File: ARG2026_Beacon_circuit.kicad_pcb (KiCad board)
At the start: 2 copper layers, 266.2 x 125.7 mm, 21 parts, among them J1 Conn_01x02_Pin, J2 Conn_01x02_Pin, Q1 IRLML0030, U1 CH32V002A4M6

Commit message: I
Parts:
- added REF**: MountingHole_3.2mm_M3, MountingHole:MountingHole_3.2mm_M3, F.Cu at (103.0, 181.4)
- added REF**: MountingHole_3.2mm_M3, MountingHole:MountingHole_3.2mm_M3, F.Cu at (81.0, 143.3)
- added REF**: MountingHole_3.2mm_M3, MountingHole:MountingHole_3.2mm_M3, F.Cu at (147.0, 181.4)
- added REF**: MountingHole_3.2mm_M3, MountingHole:MountingHole_3.2mm_M3, F.Cu at (169.0, 143.3)
- added REF**: MountingHole_3.2mm_M3, MountingHole:MountingHole_3.2mm_M3, F.Cu at (103.0, 105.3)
- added REF**: MountingHole_3.2mm_M3, MountingHole:MountingHole_3.2mm_M3, F.Cu at (147.0, 105.2)
- moved U1 92.6 mm to (150.7, 145.1)
- moved R4 91.8 mm to (143.9, 153.7)
- moved J1 91.0 mm to (151.7, 133.2)
- moved D1 90.3 mm to (91.9, 123.0)
- moved R1 90.3 mm to (101.1, 131.2)
- moved R5 90.3 mm to (96.3, 138.6)
- moved R6 90.3 mm to (90.3, 138.5)
- moved BT1 90.3 mm to (124.5, 136.9)
- moved C1 90.3 mm to (126.2, 173.3)
- moved C2 90.3 mm to (101.1, 141.1)
- moved D2 90.3 mm to (123.3, 105.1)
- moved D4 90.3 mm to (158.4, 161.4)
- moved D5 90.3 mm to (125.8, 181.6)
- moved R2 90.3 mm to (145.4, 121.7)
- moved R3 90.3 mm to (145.4, 128.6)
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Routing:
- net GND: track 0.00 -> 113.1 mm
- net /VDD: track 25.1 -> 122.9 mm
- net Net-(D1-K): track 121.9 -> 212.4 mm
- net Net-(D5-A): track 0.00 -> 44.0 mm
- net Net-(Q1-G): track 0.00 -> 19.5 mm
- net /T1C3: track 0.00 -> 12.0 mm
- net Net-(D4-A): track 0.00 -> 11.1 mm
- net /SWIO: track 0.00 -> 9.91 mm
- added copper zone on F.Cu, net GND
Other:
- board size 266.2 x 125.7 mm -> 100 x 86.6 mm

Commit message: message
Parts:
- removed the REF** at (103.0, 181.4)
- removed the REF** at (81.0, 143.3)
- removed the REF** at (147.0, 181.4)
- removed the REF** at (169.0, 143.3)
- removed the REF** at (103.0, 105.3)
- removed the REF** at (147.0, 105.2)
- added D7: LED, LED_THT:LED_D3.0mm, F.Cu at (200.2, 94.6)
- added R9: 1k, Resistor_THT:R_Axial_DIN0207_L6.3mm_D2.5mm_P10.16mm_Horizontal, F.Cu at (192.1, 94.0)
- added REF**: MountingHole_3.2mm_M3, MountingHole:MountingHole_3.2mm_M3, F.Cu at (244.1, 61.3)
- added REF**: MountingHole_3.2mm_M3, MountingHole:MountingHole_3.2mm_M3, F.Cu at (198.1, 140.9)
- added REF**: MountingHole_3.2mm_M3, MountingHole:MountingHole_3.2mm_M3, F.Cu at (267.1, 101.1)
- added REF**: MountingHole_3.2mm_M3, MountingHole:MountingHole_3.2mm_M3, F.Cu at (198.1, 61.3)
- added REF**: MountingHole_3.2mm_M3, MountingHole:MountingHole_3.2mm_M3, F.Cu at (244.1, 140.9)
- added REF**: MountingHole_3.2mm_M3, MountingHole:MountingHole_3.2mm_M3, F.Cu at (175.1, 101.1)
- added SW1: SW_SPDT, Button_Switch_THT:SW_Slide-03_Wuerth-WS-SLTV_10x2.5x6.4_P2.54mm, F.Cu at (197.6, 108.7)
- moved C2 112.1 mm to (200.5, 89.2), turned to 180 degrees
- moved R1 106.9 mm to (198.0, 86.2), turned to 90 degrees
- moved D1 104.9 mm to (188.0, 80.8)
- moved D2 104.9 mm to (219.4, 62.9)
- moved C1 104.9 mm to (222.3, 131.1)
- moved D4 104.9 mm to (254.5, 119.2)
- moved D5 104.9 mm to (221.9, 139.4)
- moved J1 104.9 mm to (247.8, 91.0)
- moved J2 104.9 mm to (247.8, 94.9)
- moved Q1 104.9 mm to (241.6, 130.3)
- moved R2 104.9 mm to (241.5, 79.5)
- moved R3 104.9 mm to (241.5, 86.5)
- moved R4 104.9 mm to (240.0, 111.6)
- moved R8 104.9 mm to (240.0, 115.2)
- moved U1 104.9 mm to (246.8, 103.0)
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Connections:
- BT1 pad 1: /VDD -> Net-(BT1-+)
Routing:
- net Net-(BT1-+): track 0.00 -> 35.7 mm
- net /VDD: track 122.9 -> 135.5 mm
- net Net-(D7-A): track 0.00 -> 11.9 mm
- net GND: track 113.1 -> 121.7 mm
- net Net-(D1-A): track 6.12 -> 14.1 mm
- net Net-(D5-A): track 44.0 -> 51.7 mm
- net Net-(D6-A): track 12.9 -> 17.3 mm

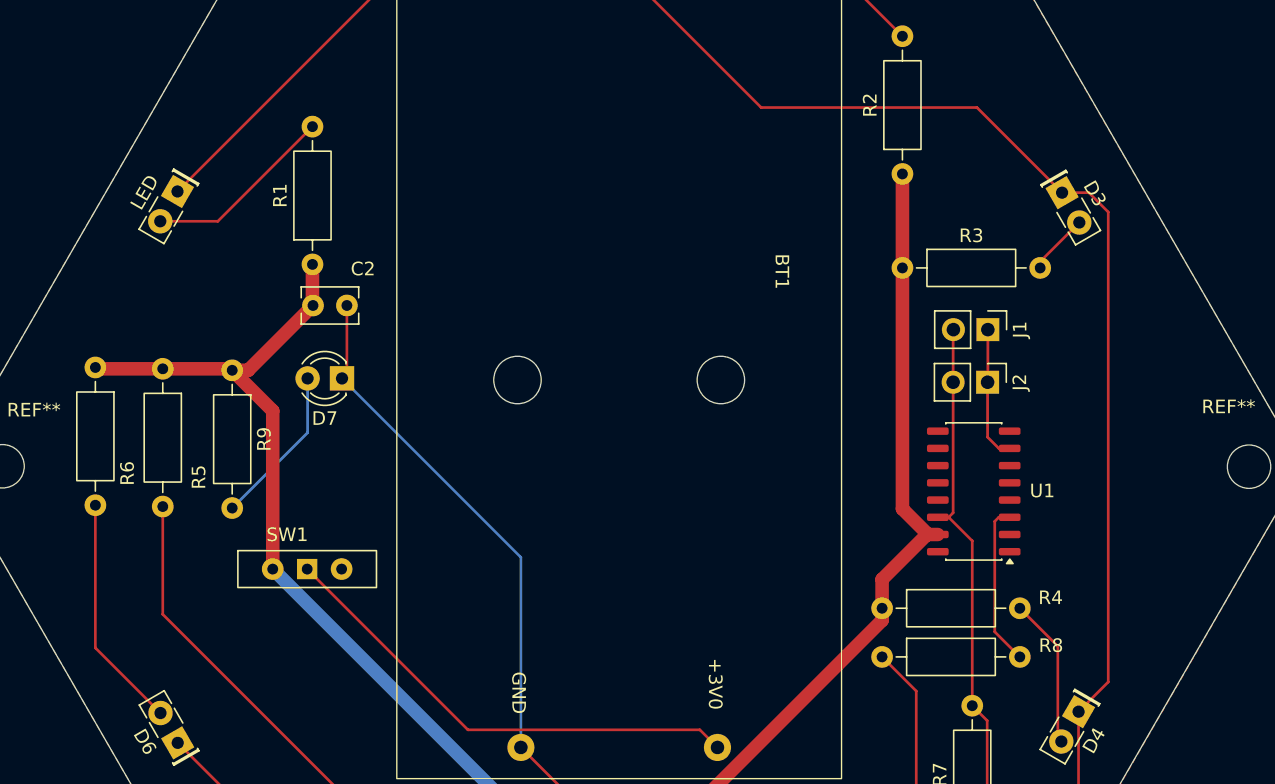
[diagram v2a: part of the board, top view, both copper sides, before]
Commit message: シルクスクリーンに値を追加、チェック
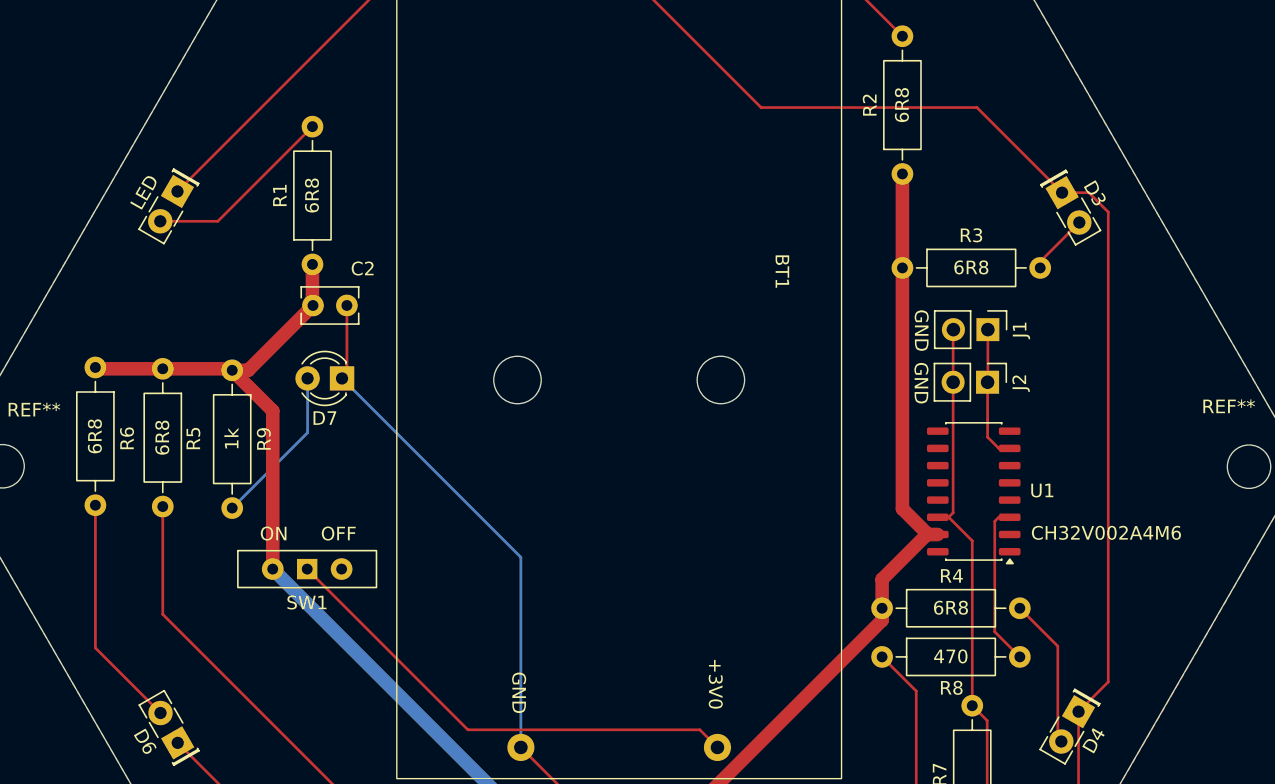
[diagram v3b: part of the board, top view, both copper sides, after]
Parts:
- R1, R2, R3, R4, R5, R6: value 5R1 -> 6R8
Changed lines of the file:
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@@
 		)
 		(property "Value" "CH32V002A4M6"
-			(at 0 5.9 0)
-			(layer "F.Fab")
+			(at -9.79 -3.09 0)
+			(layer "F.SilkS")
 			(effects
 				(font
@@
 		(tags "Resistor Axial_DIN0207 series Axial Horizontal pin pitch 10.16mm 0.25W = 1/4W length 6.3mm diameter 2.5mm")
 		(property "Reference" "R8"
-			(at 12.46 -0.83 0)
+			(at 5.12 2.316937 0)
 			(layer "F.SilkS")
 			(effects
@@
 		)
 		(property "Value" "470"
-			(at 12.78 0.93 0)
-			(layer "F.Fab")
+			(at 5.08 0 0)
+			(layer "F.SilkS")
 			(effects
 				(font
@@
 		)
 		(property "Value" "1k"
-			(at 2 -2.44 90)
-			(layer "F.Fab")
+			(at 5.08 0 90)
+			(layer "F.SilkS")
 			(effects
 				(font
@@
 			)
 		)
-		(property "Value" "5R1"
-			(at 5.08 2.37 90)
-			(layer "F.Fab")
+		(property "Value" "6R8"
+			(at 5.08 0 90)
+			(layer "F.SilkS")
 			(effects
 				(font
@@
 			(layer "F.Fab")
 		)
+		(fp_text user "GND"
+			(at -1.5 5.5 270)
+			(unlocked yes)
+			(layer "F.SilkS")
+			(effects
+				(font
+					(size 1 1)
+					(thickness 0.1)
+				)
+				(justify left bottom)
+			)
+		)
 		(fp_text user "${REFERENCE}"
 			(at 0 1.27 0)
@@
 		(tags "Resistor Axial_DIN0207 series Axial Horizontal pin pitch 10.16mm 0.25W = 1/4W length 6.3mm diameter 2.5mm")
 		(property "Reference" "R4"
-			(at 12.43 -0.77 0)
+			(at 5.12 -2.348063 0)
 			(layer "F.SilkS")
 			(effects
@@
 			)
 		)
-		(property "Value" "5R1"
-			(at 12.88 0.95 0)
-			(layer "F.Fab")
+		(property "Value" "6R8"
+			(at 5.08 0 0)
+			(layer "F.SilkS")
 			(effects
 				(font
@@
 		(tags "Resistor Axial_DIN0207 series Axial Horizontal pin pitch 10.16mm 0.25W = 1/4W length 6.3mm diameter 2.5mm")
 		(property "Reference" "R5"
-			(at 7.99 -2.67 270)
+			(at 5.15 -2.29 90)
 			(layer "F.SilkS")
 			(effects
@@
 			)
 		)
-		(property "Value" "5R1"
-			(at 3.52 -2.47 270)
-			(layer "F.Fab")
+		(property "Value" "6R8"
+			(at 5.08 0 90)
+			(layer "F.SilkS")
 			(effects
 				(font
@@
 		)
 		(property "Datasheet" ""
-			(at 0 0 270)
+			(at 0 0 90)
 			(layer "F.Fab")
 			(hide yes)
@@
 		)
 		(property "Description" "Resistor"
-			(at 0 0 270)
+			(at 0 0 90)
 			(layer "F.Fab")
 			(hide yes)
@@
 		)
 		(property "KiLib_Generator" "resistor/THT"
-			(at 0 0 270)
+			(at 0 0 90)
 			(layer "F.SilkS")
 			(hide yes)
@@
 		)
 		(fp_text user "${REFERENCE}"
-			(at 5.08 0 270)
+			(at 5.08 0 90)
 			(layer "F.Fab")
 			(effects
@@
 		(descr "Through hole straight pin header, 1x02, 2.54mm pitch, single row")
 		(tags "Through hole pin header THT 1x02 2.54mm single row")
-		(property "Reference" "J1"
-			(at 0 -2.38 90)
-			(layer "F.SilkS")
-			(effects
-				(font
-					(size 1 1)
-					(thickness 0.15)
-				)
-			)
-		)
 		(property "Value" "Conn_01x02_Pin"
 			(at 0 4.92 90)
@@
 			)
 		)
+		(property "Reference" "J1"
+			(at 0 -2.38 90)
+			(layer "F.SilkS")
+			(effects
+				(font
+					(size 1 1)
+					(thickness 0.15)
+				)
+			)
+		)
 		(property ki_fp_filters "Connector*:*_1x??_*")
 		(sheetname "/")
@@
 			(layer "F.Fab")
 		)
+		(fp_text user "GND"
+			(at -1.5 5.5 270)
+			(unlocked yes)
+			(layer "F.SilkS")
+			(effects
+				(font
+					(size 1 1)
+					(thickness 0.1)
+				)
+				(justify left bottom)
+			)
+		)
 		(fp_text user "${REFERENCE}"
 			(at 0 1.27 0)
@@
 		(tags "switch single-pole opposite-side-connection double-throw SPDT würth wurth")
 		(property "Reference" "SW1"
-			(at -1.47 -2.53 0)
+			(at 0 2.5 0)
 			(layer "F.SilkS")
 			(effects
@@
 			(layer "F.Fab")
 		)
+		(fp_text user "ON"
+			(at -3.5 -2 0)
+			(unlocked yes)
+			(layer "F.SilkS")
+			(effects
+				(font
+					(size 1 1)
+					(thickness 0.1)
+				)
+				(justify left bottom)
+			)
+		)
+		(fp_text user "OFF"
+			(at 1 -2 0)
+			(unlocked yes)
+			(layer "F.SilkS")
+			(effects
+				(font
+					(size 1 1)
+					(thickness 0.1)
+				)
+				(justify left bottom)
+			)
+		)
 		(fp_text user "${REFERENCE}"
 			(at 3.6 -2.54 0)
@@
 		(tags "Resistor Axial_DIN0207 series Axial Horizontal pin pitch 10.16mm 0.25W = 1/4W length 6.3mm diameter 2.5mm")
 		(property "Reference" "R6"
-			(at 7.81 -2.37 270)
+			(at 5.25 -2.37 90)
 			(layer "F.SilkS")
 			(effects
@@
 			)
 		)
-		(property "Value" "5R1"
-			(at 3.81 -2.38 270)
-			(layer "F.Fab")
+		(property "Value" "6R8"
+			(at 5.08 0 90)
+			(layer "F.SilkS")
 			(effects
 				(font
@@
 		)
 		(property "Datasheet" ""
-			(at 0 0 270)
+			(at 0 0 90)
 			(layer "F.Fab")
 			(hide yes)
@@
 		)
 		(property "Description" "Resistor"
-			(at 0 0 270)
+			(at 0 0 90)
 			(layer "F.Fab")
 			(hide yes)
@@
 		)
 		(property "KiLib_Generator" "resistor/THT"
-			(at 0 0 270)
+			(at 0 0 90)
 			(layer "F.SilkS")
 			(hide yes)
@@
 		)
 		(fp_text user "${REFERENCE}"
-			(at 5.08 0 270)
+			(at 5.08 0 90)
 			(layer "F.Fab")
 			(effects
@@
 			)
 		)
-		(property "Value" "5R1"
-			(at 5.08 2.37 90)
-			(layer "F.Fab")
+		(property "Value" "6R8"
+			(at 5.08 0 90)
+			(layer "F.SilkS")
 			(effects
 				(font
@@
 			)
 		)
-		(property "Value" "5R1"
-			(at 5.08 2.37 0)
-			(layer "F.Fab")
+		(property "Value" "6R8"
+			(at 5.08 0 0)
+			(layer "F.SilkS")
 			(effects
 				(font

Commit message: message
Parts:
- moved R7 30.7 mm to (261.5, 102.1), turned to 180 degrees
- moved C1 30.1 mm to (196.1, 116.2), turned to 0 degrees
- moved R8 23.6 mm to (261.4, 105.3), turned to 180 degrees
- moved Q1 14.3 mm to (245.2, 116.4)
- moved J1 13.3 mm to (246.6, 104.3)
- moved J2 13.3 mm to (246.6, 108.2)
- moved U1 8.24 mm to (245.2, 94.9)
- moved R4 1.45 mm to (241.2, 112.4)
- moved BT1 0.46 mm to (220.9, 95.0)
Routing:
- net GND: track 121.7 -> 109.4 mm
- net /VDD: track 135.5 -> 124.0 mm
- net /SWIO: track 9.91 -> 17.5 mm
- net Net-(D1-K): track 212.1 -> 205.0 mm
- net Net-(Q1-G): track 19.5 -> 22.8 mm
- net Net-(BT1-+): track 35.7 -> 38.0 mm
- net /T1C3: track 12.0 -> 10.5 mm
- net Net-(D4-A): track 11.1 -> 9.75 mm
- net Net-(D5-A): track 51.7 -> 52.6 mm

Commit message: improve silkscreen of PCB
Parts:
- added ?: , clipboard:8ea2c0b2-452e-4bc2-b55e-ed6b78fbe1c2, F.Cu at (199.4, 94.6)
- C1: value 470 -> 470u
- renumbered J2 to SWIO, J1 to SWIO

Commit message: 警告
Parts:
- moved ? 2.94 mm to (199.2, 97.5)
- moved D1 2.48 mm to (186.8, 83.0), turned to 60 degrees
- renumbered SWIO to J1, SWIO to J2
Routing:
- net Net-(D1-A): track 14.1 -> 11.9 mm
- net Net-(D1-K): track 205.0 -> 207.1 mm
- removed copper zone on F.Cu, net GND
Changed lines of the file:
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@@
 	(footprint "LED_THT:LED_Rectangular_W5.0mm_H2.0mm"
 		(layer "F.Cu")
-		(at 188.024997 80.83059 -120)
+		(at 186.815 82.999852 60)
 		(descr "LED, Rectangular, size 5.0x2.0mm, 2 pins, http://www.kingbright.com/attachments/file/psearch/000/00/00/L-169XCGDK(Ver.9B).pdf, generated by kicad-footprint-generator")
 		(tags "LED")
@@
 		)
 		(property "Sim.Pins" "1=K 2=A"
-			(at 0 0 240)
+			(at 0 0 60)
 			(unlocked yes)
 			(layer "F.Fab")
@@
 		(sheetname "/")
 		(sheetfile "ARG2026_Beacon_circuit.kicad_sch")
+		(units
+			(unit
+				(name "A")
+				(pins "1" "2")
+			)
+		)
 		(attr through_hole)
 		(duplicate_pad_numbers_are_jumpers no)
 		(fp_line
-			(start 3.83 1.06)
-			(end 2.747 1.06)
+			(start -1.29 -1.06)
+			(end -1.08 -1.06)
 			(stroke
 				(width 0.12)
@@
 		)
 		(fp_line
-			(start 2.333 1.06)
-			(end 1.08 1.06)
+			(start -1.17 -1.06)
+			(end -1.17 1.06)
 			(stroke
 				(width 0.12)
@@
 		)
 		(fp_line
-			(start 0.551733 2)
-			(end 0.551733 2.448267)
+			(start 1.08 -1.06)
+			(end 2.333 -1.06)
 			(stroke
-				(width 0.070576)
-				(type default)
+				(width 0.12)
+				(type solid)
 			)
 			(layer "F.SilkS")
 		)
 		(fp_line
-			(start 0.551733 2)
-			(end 0.103404 2)
+			(start -1.29 1.06)
+			(end -1.29 -1.06)
 			(stroke
-				(width 0.070576)
-				(type default)
+				(width 0.12)
+				(type solid)
 			)
 			(layer "F.SilkS")
 		)
 		(fp_line
-			(start 0.551733 2)
-			(end 0.551733 1.551733)
+			(start -1.08 1.06)
+			(end -1.29 1.06)
 			(stroke
-				(width 0.070576)
-				(type default)
+				(width 0.12)
+				(type solid)
 			)
 			(layer "F.SilkS")
 		)
 		(fp_line
-			(start 0.103404 2)
-			(end -0.344889 2)
+			(start 2.747 -1.06)
+			(end 3.83 -1.06)
 			(stroke
-				(width 0.070576)
-				(type default)
+				(width 0.12)
+				(type solid)
 			)
 			(layer "F.SilkS")
 		)
 		(fp_line
-			(start -0.344889 2)
-			(end 2.344888 2)
+			(start 3.83 -1.06)
+			(end 3.83 1.06)
 			(stroke
-				(width 0.070576)
-				(type default)
+				(width 0.12)
+				(type solid)
 			)
 			(layer "F.SilkS")
 		)
 		(fp_line
-			(start 3.83 -1.06)
-			(end 3.83 1.06)
+			(start -0.344889 2)
+			(end 2.344888 2)
 			(stroke
-				(width 0.12)
-				(type solid)
+				(width 0.070576)
+				(type default)
 			)
 			(layer "F.SilkS")
 		)
 		(fp_line
-			(start 2.747 -1.06)
-			(end 3.83 -1.06)
+			(start 0.103404 2)
+			(end -0.344889 2)
 			(stroke
-				(width 0.12)
-				(type solid)
+				(width 0.070576)
+				(type default)
 			)
 			(layer "F.SilkS")
 		)
 		(fp_line
-			(start -1.08 1.06)
-			(end -1.29 1.06)
+			(start 0.551733 2)
+			(end 0.551733 1.551733)
 			(stroke
-				(width 0.12)
-				(type solid)
+				(width 0.070576)
+				(type default)
 			)
 			(layer "F.SilkS")
 		)
 		(fp_line
-			(start -1.29 1.06)
-			(end -1.29 -1.06)
+			(start 0.551733 2)
+			(end 0.103404 2)
 			(stroke
-				(width 0.12)
-				(type solid)
+				(width 0.070576)
+				(type default)
 			)
 			(layer "F.SilkS")
 		)
 		(fp_line
-			(start 1.08 -1.06)
-			(end 2.333 -1.06)
+			(start 0.551733 2)
+			(end 0.551733 2.448267)
 			(stroke
-				(width 0.12)
-				(type solid)
+				(width 0.070576)
+				(type default)
 			)
 			(layer "F.SilkS")
 		)
 		(fp_line
-			(start -1.17 -1.06)
-			(end -1.17 1.06)
+			(start 2.333 1.06)
+			(end 1.08 1.06)
 			(stroke
 				(width 0.12)
@@
 		)
 		(fp_line
-			(start -1.29 -1.06)
-			(end -1.08 -1.06)
+			(start 3.83 1.06)
+			(end 2.747 1.06)
 			(stroke
 				(width 0.12)
@@
 		)
 		(point
-			(at 187.389997 81.930442)
+			(at 187.45 81.9)
 			(size 2)
 			(layer "F.Fab")
 		)
 		(pad "1" thru_hole rect
-			(at 0 0 240)
+			(at 0 0 60)
 			(size 1.8 1.8)
 			(drill 0.9)
@@
 		)
 		(pad "2" thru_hole circle
-			(at 2.54 0 240)
+			(at 2.54 0 60)
 			(size 1.8 1.8)
 			(drill 0.9)
@@
 		(sheetname "/")
 		(sheetfile "ARG2026_Beacon_circuit.kicad_sch")
+		(units
+			(unit
+				(name "A")
+				(pins "1" "2")
+			)
+		)
 		(attr through_hole)
 		(duplicate_pad_numbers_are_jumpers no)
@@
 		)
 		(fp_text user "${REFERENCE}"
-			(at 1.27 0 0)
+			(at -2.37 0.04 0)
 			(layer "F.Fab")
 			(effects
@@
 	(footprint "clipboard:8ea2c0b2-452e-4bc2-b55e-ed6b78fbe1c2"
 		(layer "F.Cu")
-		(at 199.39 94.615 180)
+		(at 199.238267 97.55 180)
 		(property "Reference" ""
 			(at 0 0 0)
@@
 		(descr "Through hole straight pin header, 1x02, 2.54mm pitch, single row")
 		(tags "Through hole pin header THT 1x02 2.54mm single row")
-		(property "Reference" "SWIO"
+		(property "Reference" "J2"
 			(at 0 -2.38 90)
 			(layer "F.SilkS")
@@
 		(sheetname "/")
 		(sheetfile "ARG2026_Beacon_circuit.kicad_sch")
+		(units
+			(unit
+				(name "A")
+				(pins "1" "2")
+			)
+		)
 		(attr through_hole)
 		(duplicate_pad_numbers_are_jumpers no)
@@
 		(descr "Through hole straight pin header, 1x02, 2.54mm pitch, single row")
 		(tags "Through hole pin header THT 1x02 2.54mm single row")
-		(property "Reference" "SWIO"
+		(property "Reference" "J1"
 			(at 0 -2.38 90)
 			(layer "F.SilkS")
@@
 		(sheetname "/")
 		(sheetfile "ARG2026_Beacon_circuit.kicad_sch")
+		(units
+			(unit
+				(name "A")
+				(pins "1" "2")
+			)
+		)
 		(attr through_hole)
 		(duplicate_pad_numbers_are_jumpers no)
@@
 		)
 		(fp_text user "${REFERENCE}"
-			(at 1.27 0 60)
+			(at -2.407271 0.027042 60)
 			(layer "F.Fab")
 			(effects
@@
 		(sheetname "/")
 		(sheetfile "ARG2026_Beacon_circuit.kicad_sch")
+		(units
+			(unit
+				(name "A")
+				(pins "1" "2")
+			)
+		)
 		(attr through_hole)
 		(duplicate_pad_numbers_are_jumpers no)
@@
 		)
 		(fp_text user "${REFERENCE}"
-			(at 1.27 0 120)
+			(at 5.213768 0.129193 120)
 			(layer "F.Fab")
 			(effects
@@
 		(sheetname "/")
 		(sheetfile "ARG2026_Beacon_circuit.kicad_sch")
+		(units
+			(unit
+				(name "A")
+				(pins "1" "2")
+			)
+		)
 		(attr through_hole)
 		(duplicate_pad_numbers_are_jumpers no)
@@
 		)
 		(fp_text user "${REFERENCE}"
-			(at 1.27 0 120)
+			(at -2.511588 -0.517242 120)
 			(layer "F.Fab")
 			(effects
@@
 		(tags "LED")
 		(property "Reference" "D7"
-			(at 1.27 -2.96 0)
+			(at -2.41 0.75 0)
 			(layer "F.SilkS")
 			(effects
@@
 	)
 	(segment
-		(start 188.024997 80.83059)
-		(end 205.925587 62.93)
+		(start 219.36 62.93)
+		(end 219.36 64.91)
 		(width 0.5)
 		(layer "F.Cu")
@@
 	)
 	(segment
-		(start 219.36 62.93)
-		(end 219.36 64.91)
+		(start 199.290148 82.999852)
+		(end 186.815 82.999852)
 		(width 0.5)
 		(layer "F.Cu")
@@
 	)
 	(segment
-		(start 205.925587 62.93)
-		(end 219.36 62.93)
+		(start 219.36 62.93)
+		(end 199.290148 82.999852)
 		(width 0.5)
 		(layer "F.Cu")
@@
 	)
 	(segment
-		(start 190.999705 83.030295)
-		(end 197.98 76.05)
-		(width 1.5)
+		(start 188.085 80.800147)
+		(end 193.229853 80.800147)
+		(width 1)
 		(layer "F.Cu")
 		(net "Net-(D1-A)")
 	)
 	(segment
-		(start 186.754997 83.030295)
-		(end 190.999705 83.030295)
-		(width 1.5)
+		(start 193.229853 80.800147)
+		(end 197.98 76.05)
+		(width 1)
 		(layer "F.Cu")
 		(net "Net-(D1-A)")
@@
 	)
 	(zone
-		(net "GND")
-		(layer "F.Cu")
-		(hatch edge 0.5)
-		(connect_pads
-			(clearance 0.5)
-		)
-		(min_thickness 0.25)
-		(fill yes
-			(thermal_gap 0.5)
-			(thermal_bridge_width 0.5)
-			(island_removal_mode 0)
-		)
-		(polygon
-			(pts
-				(xy 196.06 57.82) (xy 246.05 57.81) (xy 271.06 101.128086) (xy 246.08 144.39) (xy 196.08 144.41)
-				(xy 171.07 101.098086)
-			)
-		)
-	)
-	(zone
